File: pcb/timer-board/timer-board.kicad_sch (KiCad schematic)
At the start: 0 parts

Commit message: Start schematic design of the timer board, add MCU, USB, IR receiver and OLED
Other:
- added sheet Display (display.kicad_sch)
- added sheet IR receiver (ir-receiver.kicad_sch)
- added sheet MCU (mcu.kicad_sch)
- added sheet Power (power.kicad_sch)
- added sheet USB (usb.kicad_sch)

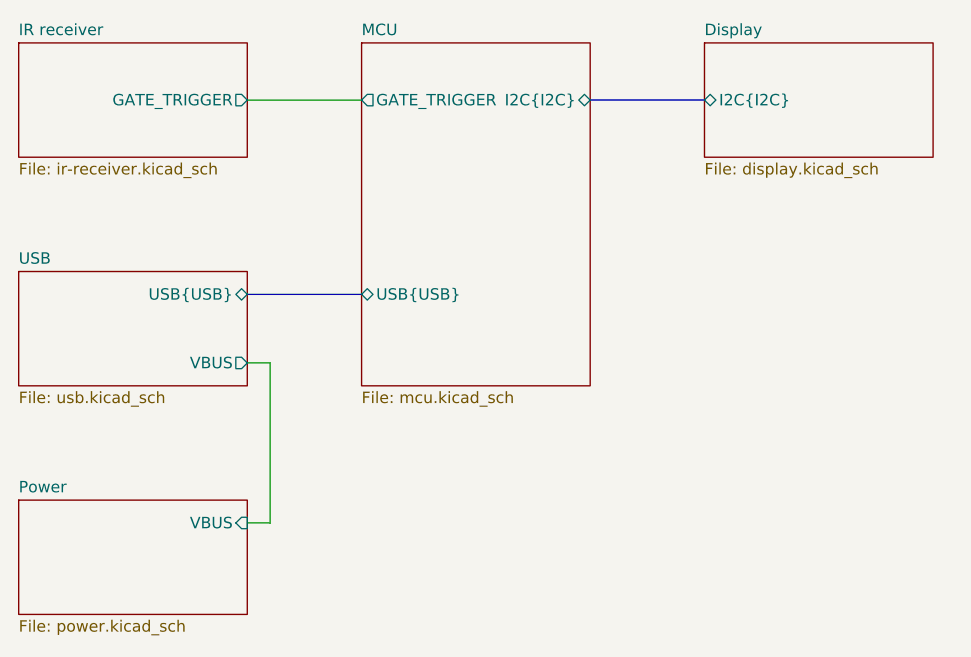
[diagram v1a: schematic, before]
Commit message: Connect OLED display, position main components
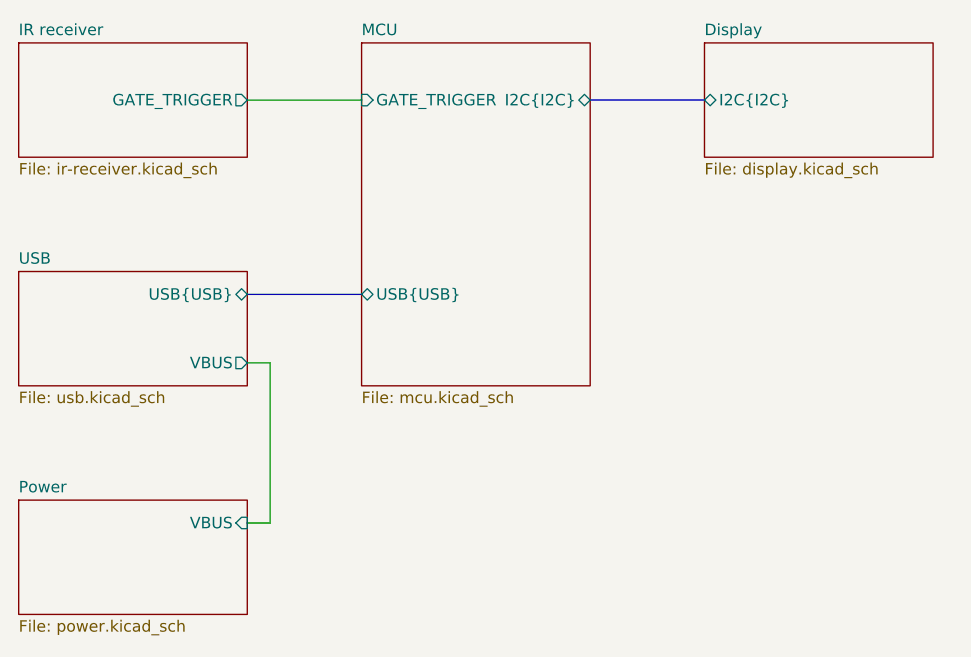
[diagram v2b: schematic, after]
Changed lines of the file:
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@@
 			)
 		)
-		(pin "GATE_TRIGGER" output
-			(at 127 82.55 180)
+		(pin "USB{USB}" bidirectional
+			(at 127 104.14 180)
 			(effects
 				(font
@@
 			)
 		)
-		(pin "USB{USB}" bidirectional
-			(at 127 104.14 180)
+		(pin "GATE_TRIGGER" input
+			(at 127 82.55 180)
 			(effects
 				(font

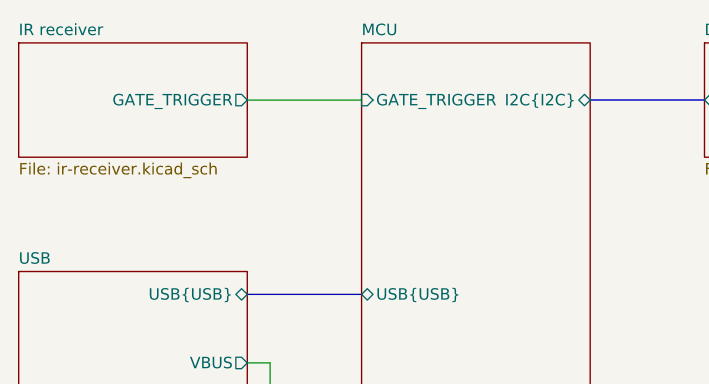
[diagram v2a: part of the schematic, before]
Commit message: Add 3.5mm jack, fix BOOT0 connection
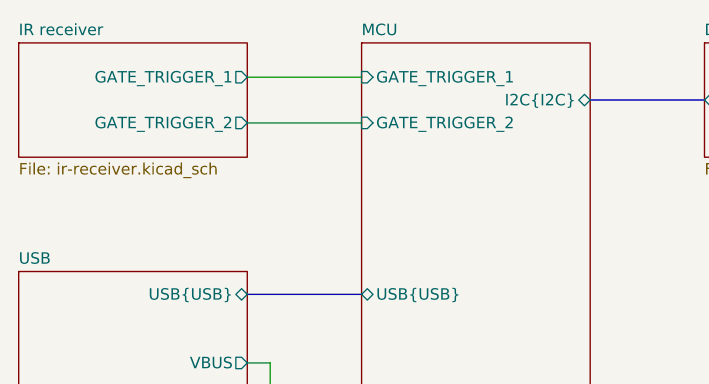
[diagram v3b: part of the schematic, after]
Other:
- sheet IR receiver ports: added GATE_TRIGGER_1, GATE_TRIGGER_2; removed GATE_TRIGGER
- sheet MCU ports: added GATE_TRIGGER_1, GATE_TRIGGER_2; removed GATE_TRIGGER
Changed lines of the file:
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@@
+	(wire
+		(pts
+			(xy 114.3 85.09) (xy 127 85.09)
+		)
+		(stroke
+			(width 0)
+			(type default)
+		)
+	)
 	(wire
 		(pts
@@
 	(wire
 		(pts
-			(xy 114.3 82.55) (xy 127 82.55)
+			(xy 114.3 80.01) (xy 127 80.01)
 		)
 		(stroke
@@
 			)
 		)
-		(pin "GATE_TRIGGER" input
-			(at 127 82.55 180)
+		(pin "GATE_TRIGGER_1" input
+			(at 127 80.01 180)
+			(effects
+				(font
+					(size 1.27 1.27)
+				)
+				(justify left)
+			)
+		)
+		(pin "GATE_TRIGGER_2" input
+			(at 127 85.09 180)
 			(effects
 				(font
@@
 			)
 		)
-		(pin "GATE_TRIGGER" output
-			(at 114.3 82.55 0)
+		(pin "GATE_TRIGGER_1" output
+			(at 114.3 80.01 0)
 			(effects
 				(font
+					(size 1.27 1.27)
+				)
+				(justify right)
+			)
+		)
+		(pin "GATE_TRIGGER_2" output
+			(at 114.3 85.09 0)
+			(effects
+				(font

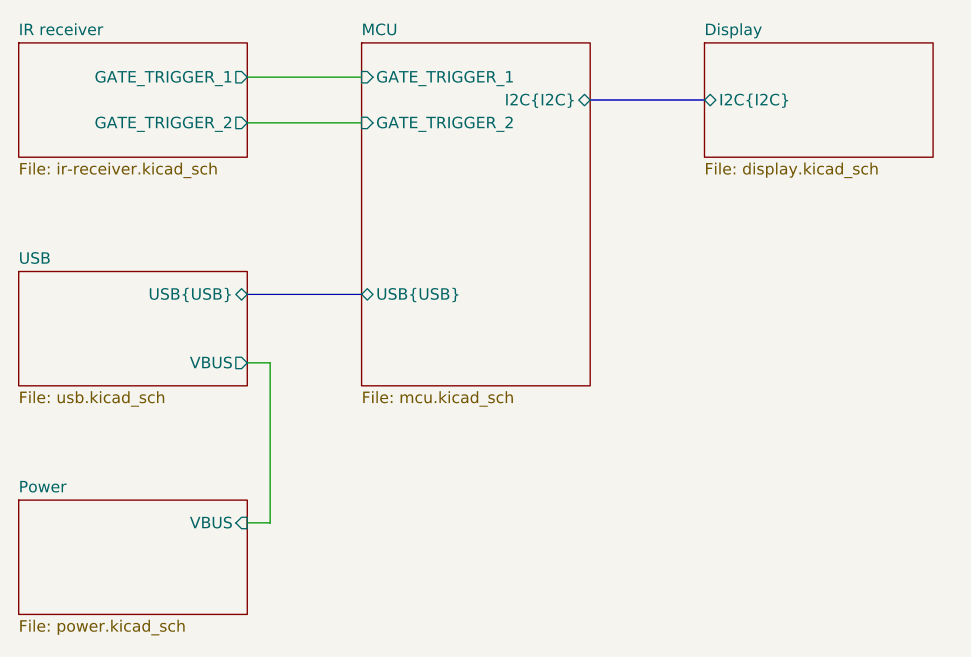
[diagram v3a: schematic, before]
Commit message: Add I2C pull-up, IR receiver decoupling, LED labels, clear ERC and DRC
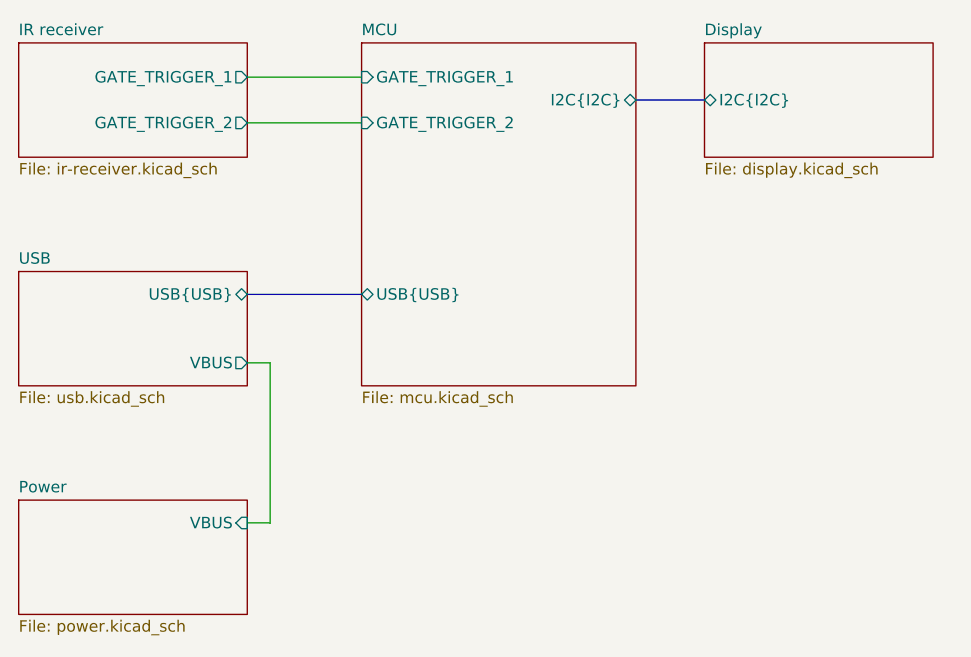
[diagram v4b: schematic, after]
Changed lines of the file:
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@@
+		)
+	)
+	(bus
+		(pts
+			(xy 157.48 82.55) (xy 165.1 82.55)
+		)
+		(stroke
+			(width 0)
+			(type default)
 		)
 	)
@@
 		)
 	)
-	(bus
-		(pts
-			(xy 152.4 82.55) (xy 165.1 82.55)
-		)
-		(stroke
-			(width 0)
-			(type default)
-		)
-	)
 	(wire
 		(pts
@@
 	(sheet
 		(at 127 76.2)
-		(size 25.4 38.1)
+		(size 30.48 38.1)
 		(exclude_from_sim no)
 		(in_bom yes)
@@
 		)
 		(pin "I2C{I2C}" bidirectional
-			(at 152.4 82.55 0)
+			(at 157.48 82.55 0)
 			(effects
 				(font
